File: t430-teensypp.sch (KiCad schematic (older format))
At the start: 0 parts

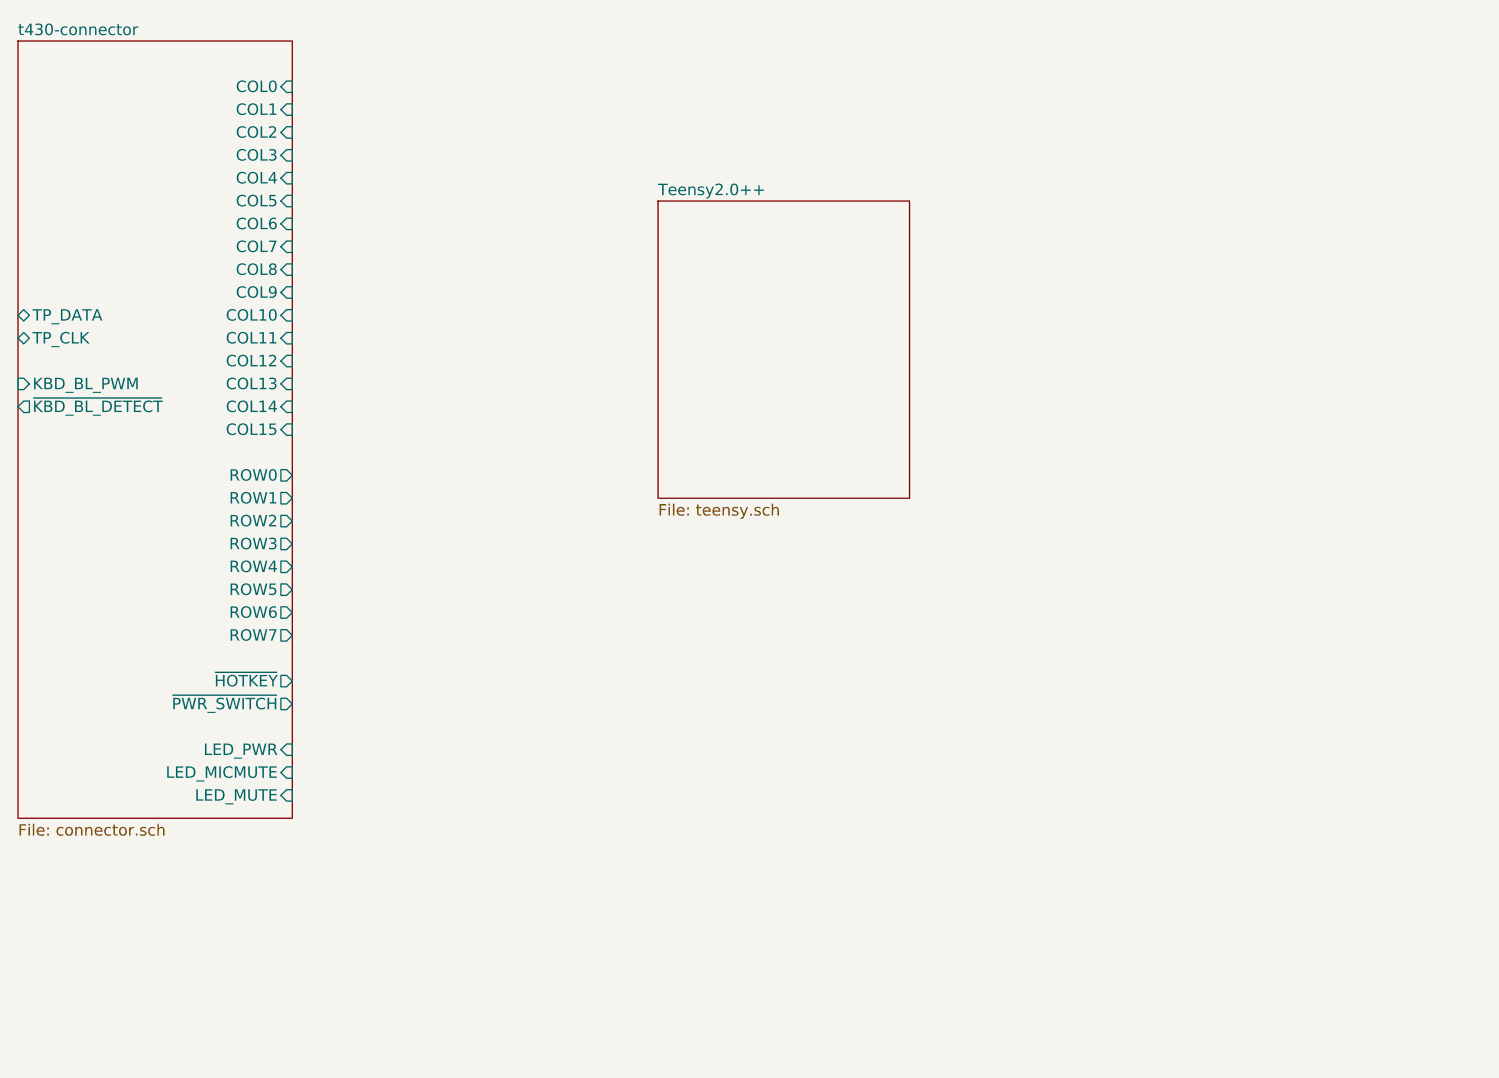
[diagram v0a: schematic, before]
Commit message: Updated footprints and started PCB
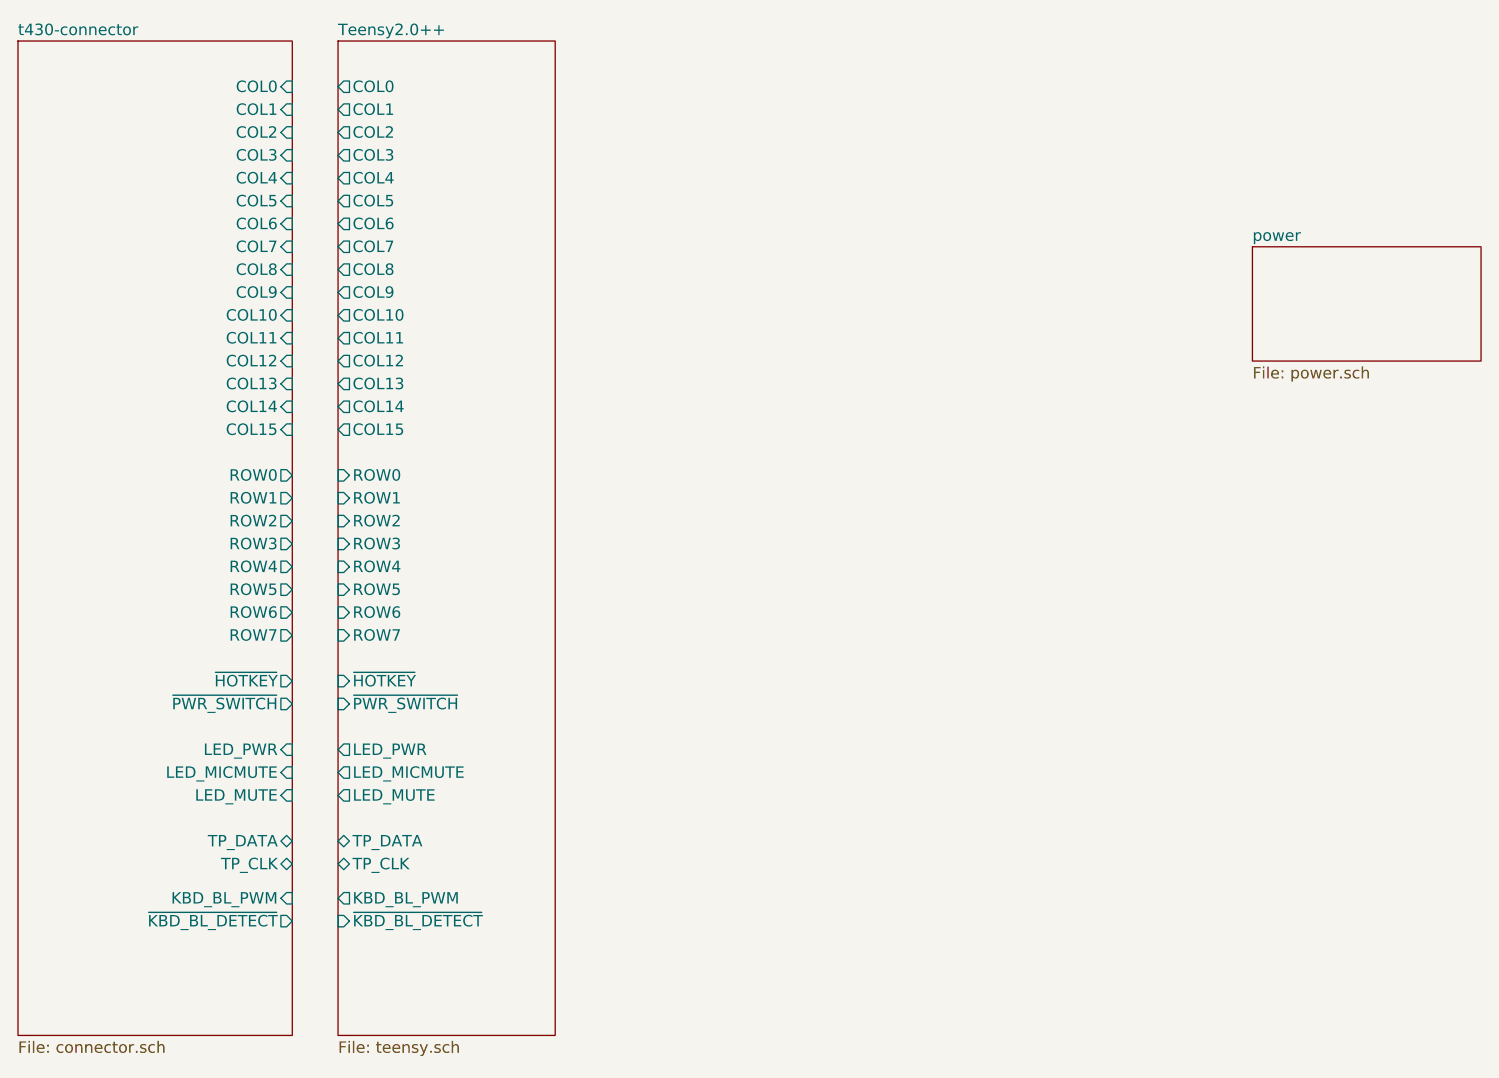
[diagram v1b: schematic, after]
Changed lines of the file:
@@
 $Descr A4 11693 8268
 encoding utf-8
-Sheet 1 3
+Sheet 1 4
 Title ""
 Date ""
@@
 $EndDescr
 $Sheet
-S 3200 1500 1200 3400
+S 3200 1500 1200 4350
 U 5D4876A5
 F0 "t430-connector" 50
@@
 F26 "~HOTKEY" O R 4400 4300 50
 F27 "~PWR_SWITCH" O R 4400 4400 50
-F28 "KBD_BL_PWM" I L 3200 3000 50
-F29 "~KBD_BL_DETECT" O L 3200 3100 50
-F30 "TP_DATA" B L 3200 2700 50
-F31 "TP_CLK" B L 3200 2800 50
+F28 "KBD_BL_PWM" I R 4400 5250 50
+F29 "~KBD_BL_DETECT" O R 4400 5350 50
+F30 "TP_DATA" B R 4400 5000 50
+F31 "TP_CLK" B R 4400 5100 50
 F32 "LED_PWR" I R 4400 4600 50
 F33 "LED_MICMUTE" I R 4400 4700 50
@@
 $EndSheet
 $Sheet
-S 6000 2200 1100 1300
+S 4600 1500 950  4350
 U 5D54C373
 F0 "Teensy2.0++" 50
 F1 "teensy.sch" 50
+F2 "ROW0" I L 4600 3400 50
+F3 "ROW1" I L 4600 3500 50
+F4 "ROW2" I L 4600 3600 50
+F5 "ROW3" I L 4600 3700 50
+F6 "ROW4" I L 4600 3800 50
+F7 "ROW5" I L 4600 3900 50
+F8 "ROW6" I L 4600 4000 50
+F9 "ROW7" I L 4600 4100 50
+F10 "TP_CLK" B L 4600 5100 50
+F11 "TP_DATA" B L 4600 5000 50
+F12 "~HOTKEY" I L 4600 4300 50
+F13 "~PWR_SWITCH" I L 4600 4400 50
+F14 "KBD_BL_PWM" O L 4600 5250 50
+F15 "~KBD_BL_DETECT" I L 4600 5350 50
+F16 "LED_PWR" O L 4600 4600 50
+F17 "LED_MICMUTE" O L 4600 4700 50
+F18 "LED_MUTE" O L 4600 4800 50
+F19 "COL0" O L 4600 1700 50
+F20 "COL1" O L 4600 1800 50
+F21 "COL2" O L 4600 1900 50
+F22 "COL4" O L 4600 2100 50
+F23 "COL5" O L 4600 2200 50
+F24 "COL6" O L 4600 2300 50
+F25 "COL7" O L 4600 2400 50
+F26 "COL8" O L 4600 2500 50
+F27 "COL9" O L 4600 2600 50
+F28 "COL10" O L 4600 2700 50
+F29 "COL11" O L 4600 2800 50
+F30 "COL12" O L 4600 2900 50
+F31 "COL13" O L 4600 3000 50
+F32 "COL14" O L 4600 3100 50
+F33 "COL15" O L 4600 3200 50
+F34 "COL3" O L 4600 2000 50
+$EndSheet
+$Sheet
+S 8600 2400 1000 500
+U 5D491B51
+F0 "power" 50
+F1 "power.sch" 50
 $EndSheet
 $EndSCHEMATC

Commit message: Routed to 6/6
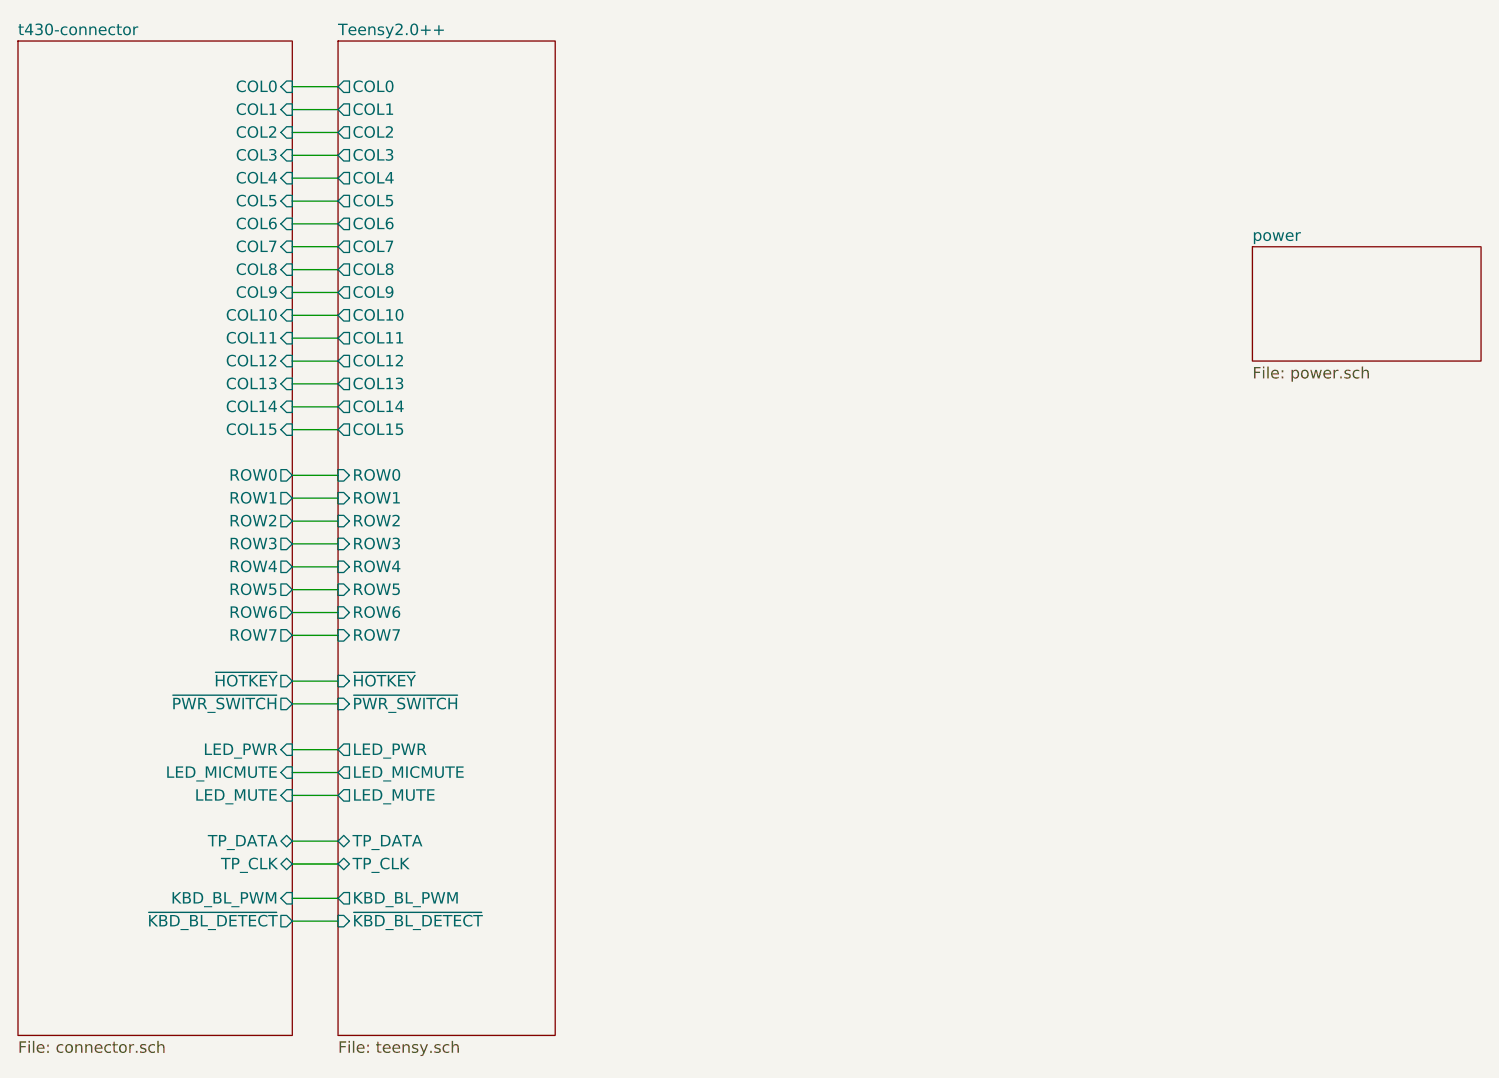
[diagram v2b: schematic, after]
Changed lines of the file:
@@
 F1 "power.sch" 50
 $EndSheet
+Wire Wire Line
+	4400 1700 4600 1700
+Wire Wire Line
+	4600 1800 4400 1800
+Wire Wire Line
+	4400 1900 4600 1900
+Wire Wire Line
+	4600 2000 4400 2000
+Wire Wire Line
+	4400 2100 4600 2100
+Wire Wire Line
+	4600 2200 4400 2200
+Wire Wire Line
+	4400 2300 4600 2300
+Wire Wire Line
+	4600 2400 4400 2400
+Wire Wire Line
+	4400 2500 4600 2500
+Wire Wire Line
+	4600 2600 4400 2600
+Wire Wire Line
+	4400 2700 4600 2700
+Wire Wire Line
+	4600 2800 4400 2800
+Wire Wire Line
+	4400 2900 4600 2900
+Wire Wire Line
+	4600 3000 4400 3000
+Wire Wire Line
+	4400 3100 4600 3100
+Wire Wire Line
+	4600 3200 4400 3200
+Wire Wire Line
+	4400 5350 4600 5350
+Wire Wire Line
+	4400 3400 4600 3400
+Wire Wire Line
+	4600 3500 4400 3500
+Wire Wire Line
+	4400 3600 4600 3600
+Wire Wire Line
+	4600 3700 4400 3700
+Wire Wire Line
+	4400 3800 4600 3800
+Wire Wire Line
+	4600 3900 4400 3900
+Wire Wire Line
+	4400 4000 4600 4000
+Wire Wire Line
+	4600 4100 4400 4100
+Wire Wire Line
+	4400 5000 4600 5000
+Wire Wire Line
+	4600 5100 4400 5100
+Wire Wire Line
+	4400 5250 4600 5250
+Wire Wire Line
+	4600 4800 4400 4800
+Wire Wire Line
+	4400 4700 4600 4700
+Wire Wire Line
+	4600 4600 4400 4600
+Wire Wire Line
+	4400 4400 4600 4400
+Wire Wire Line
+	4600 4300 4400 4300
 $EndSCHEMATC
